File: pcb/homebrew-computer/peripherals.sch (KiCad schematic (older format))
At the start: 0 parts

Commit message: Add the memory interface logic
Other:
- note added: "This part needs to include logic for handling peripheral interrupts"
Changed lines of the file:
@@
 Comment4 ""
 $EndDescr
+Text Notes 3250 2850 0    50   Italic 0
+This part needs to include logic for handling peripheral interrupts
 $EndSCHEMATC

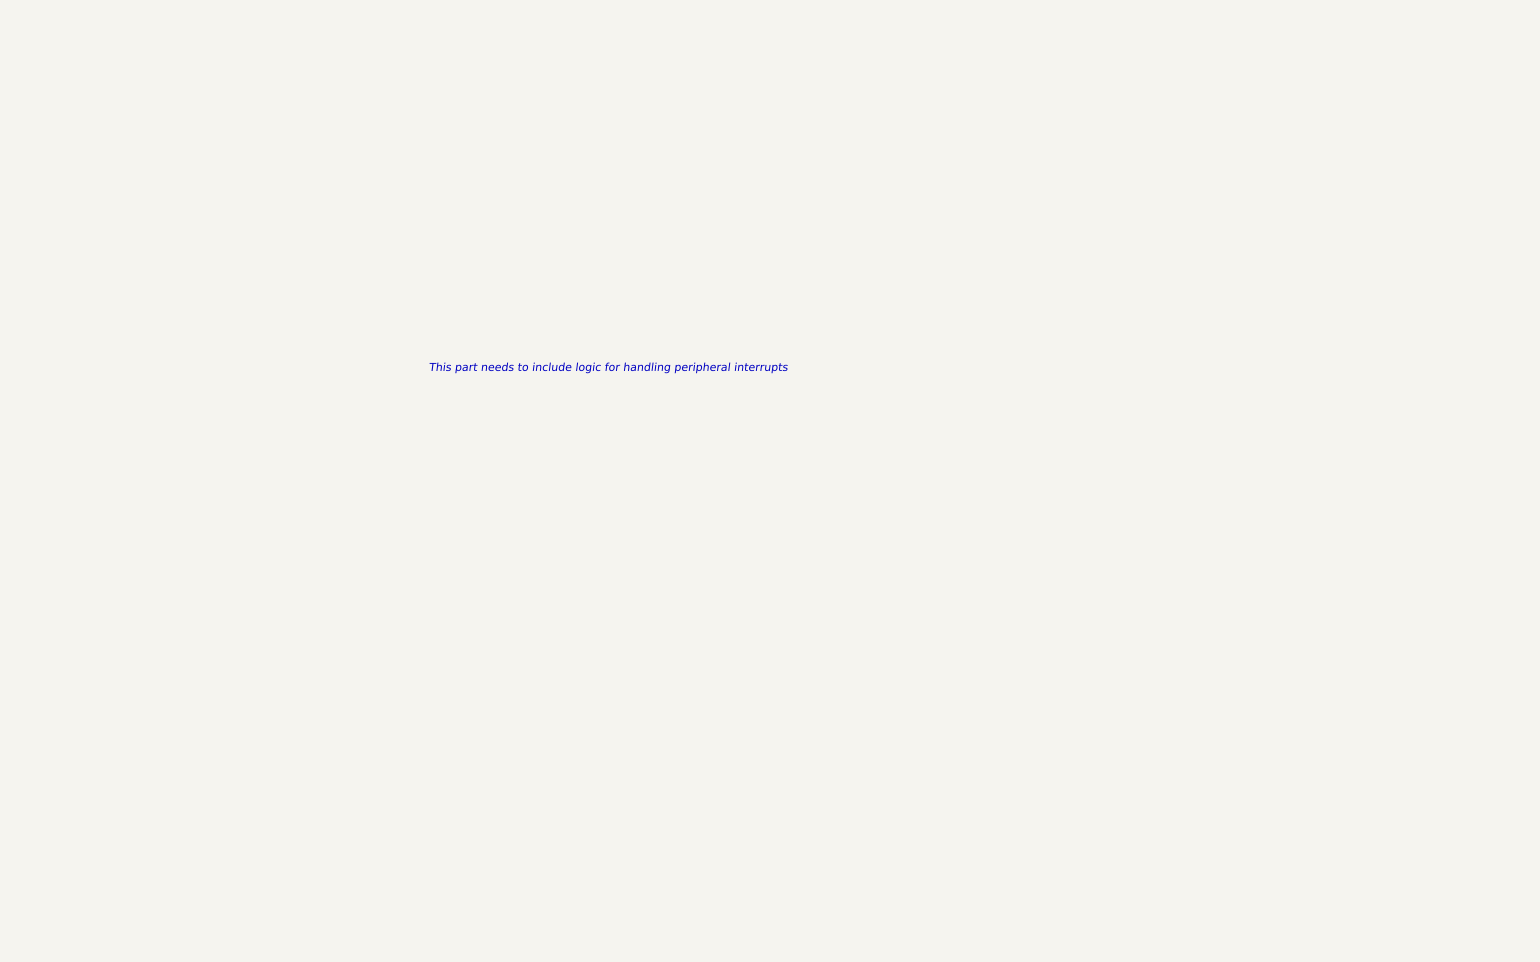
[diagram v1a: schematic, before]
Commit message: Add beginning of peripheral ios
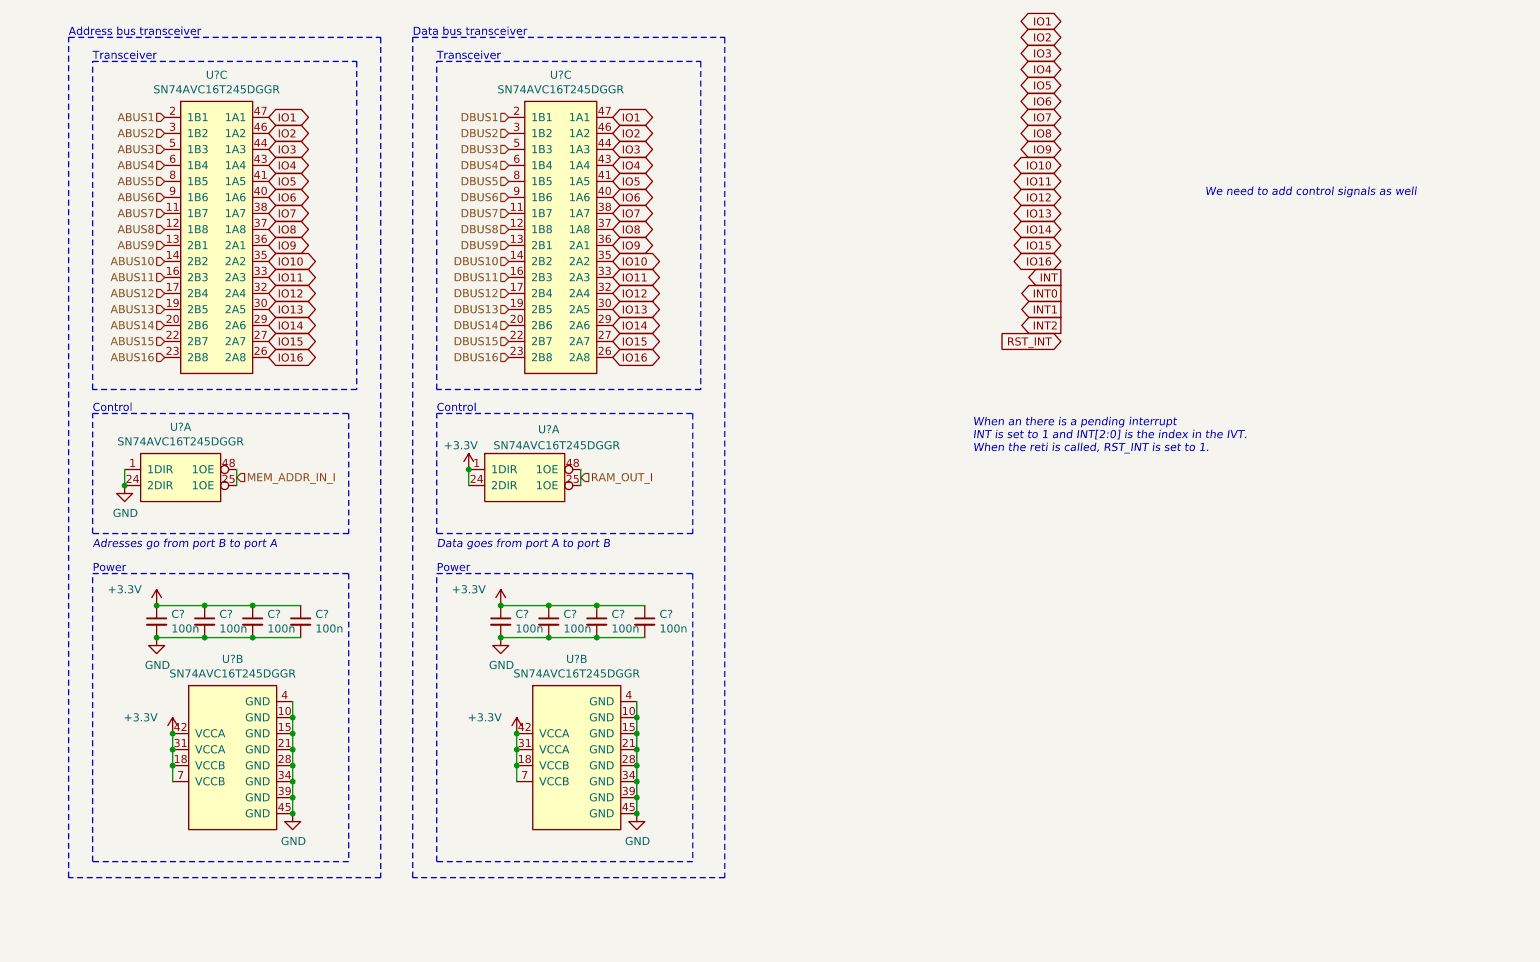
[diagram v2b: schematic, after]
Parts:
- added C? (x8): 100n, symbol Device:C_Small
- added U? (x6): SN74AVC16T245DGGR, symbol 74AVC16T245:SN74AVC16T245DGGR
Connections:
- new net +3V3: C?.1, C?.1, C?.1, C?.1, C?.1, C?.1, C?.1, C?.1, U?.1 (1DIR), U?.18 (VCCB), U?.18 (VCCB), U?.24 (2DIR), U?.31 (VCCA), U?.31 (VCCA), U?.42 (VCCA), U?.42 (VCCA), U?.7 (VCCB), U?.7 (VCCB)
- new net ABUS1: U?.2 (1B1)
- new net ABUS10: U?.14 (2B2)
- new net ABUS11: U?.16 (2B3)
- new net ABUS12: U?.17 (2B4)
- new net ABUS13: U?.19 (2B5)
- new net ABUS14: U?.20 (2B6)
- new net ABUS15: U?.22 (2B7)
- new net ABUS16: U?.23 (2B8)
- new net ABUS2: U?.3 (1B2)
- new net ABUS3: U?.5 (1B3)
- new net ABUS4: U?.6 (1B4)
- new net ABUS5: U?.8 (1B5)
- new net ABUS6: U?.9 (1B6)
- new net ABUS7: U?.11 (1B7)
- new net ABUS8: U?.12 (1B8)
- new net ABUS9: U?.13 (2B1)
- new net DBUS1: U?.2 (1B1)
- new net DBUS10: U?.14 (2B2)
- new net DBUS11: U?.16 (2B3)
- new net DBUS12: U?.17 (2B4)
- new net DBUS13: U?.19 (2B5)
- new net DBUS14: U?.20 (2B6)
- new net DBUS15: U?.22 (2B7)
- new net DBUS16: U?.23 (2B8)
- new net DBUS2: U?.3 (1B2)
- new net DBUS3: U?.5 (1B3)
- new net DBUS4: U?.6 (1B4)
- new net DBUS5: U?.8 (1B5)
- new net DBUS6: U?.9 (1B6)
- new net DBUS7: U?.11 (1B7)
- new net DBUS8: U?.12 (1B8)
- new net DBUS9: U?.13 (2B1)
- new net GND: C?.2, C?.2, C?.2, C?.2, C?.2, C?.2, C?.2, C?.2, U?.1 (1DIR), U?.10 (GND), U?.10 (GND), U?.15 (GND), U?.15 (GND), U?.21 (GND), U?.21 (GND), U?.24 (2DIR), U?.28 (GND), U?.28 (GND), U?.34 (GND), U?.34 (GND), U?.39 (GND), U?.39 (GND), U?.4 (GND), U?.4 (GND), U?.45 (GND), U?.45 (GND)
- new net IO1: U?.47 (1A1), U?.47 (1A1)
- new net IO10: U?.35 (2A2), U?.35 (2A2)
- new net IO11: U?.33 (2A3), U?.33 (2A3)
- new net IO12: U?.32 (2A4), U?.32 (2A4)
- new net IO13: U?.30 (2A5), U?.30 (2A5)
- new net IO14: U?.29 (2A6), U?.29 (2A6)
- new net IO15: U?.27 (2A7), U?.27 (2A7)
- new net IO16: U?.26 (2A8), U?.26 (2A8)
- new net IO2: U?.46 (1A2), U?.46 (1A2)
- new net IO3: U?.44 (1A3), U?.44 (1A3)
- new net IO4: U?.43 (1A4), U?.43 (1A4)
- new net IO5: U?.41 (1A5), U?.41 (1A5)
- new net IO6: U?.40 (1A6), U?.40 (1A6)
- new net IO7: U?.38 (1A7), U?.38 (1A7)
- new net IO8: U?.37 (1A8), U?.37 (1A8)
- new net IO9: U?.36 (2A1), U?.36 (2A1)
- new net MEM_ADDR_IN_I: U?.25 (1OE), U?.48 (1OE)
- new net RAM_OUT_I: U?.25 (1OE), U?.48 (1OE)
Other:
- note added: "Address bus transceiver"
- note added: "Adresses go from port B to port A"
- note added: "Control"
- note added: "Data bus transceiver"
- note added: "Data goes from port A to port B"
- note added: "Power"
- note added: "Transceiver"
- note added: "We need to add control signals as well"
- note added: "When an there is a pending interrupt\nINT is set to 1 and INT[2:0] is the index in the IVT.\nWhen the reti is called, RST_INT is set to 1."
- note removed: "This part needs to include logic for handling peripheral interrupts"

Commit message: Keep working on the peripheral interface
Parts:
- removed C? (x4): 100n, symbol Device:C_Small
- removed U? (x3): SN74AVC16T245DGGR, symbol 74AVC16T245:SN74AVC16T245DGGR
- added C? (x5): 100n, symbol Device:C_Small
- added D? (x4): D_Small, symbol Device:D_Small
- added J?: Conn_02x20_Counter_Clockwise, symbol Connector_Generic:Conn_02x20_Counter_Clockwise
- added U?: SN74AVC4T245PWR, symbol 74AVC4T245:SN74AVC4T245PWR
- added U? (x3): SN74AVC16T245DGGR, symbol 74AVC16T245:SN74AVC16T245DGGR
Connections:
- net +3V3: now also C?.1, C?.1, C?.1, C?.1, C?.1, U?.1 (1DIR), U?.1 (VCCA), U?.16 (VCCB), U?.18 (VCCB), U?.2 (1DIR), U?.24 (2DIR), U?.3 (2DIR), U?.31 (VCCA), U?.42 (VCCA), U?.7 (VCCB)
- net ABUS1: now also U?.13 (1B1)
- net ABUS2: now also U?.12 (1B2)
- net ABUS3: now also U?.11 (2B1)
- net DBUS1: now also U?.2 (1B1)
- net DBUS10: now also U?.14 (2B2)
- net DBUS11: now also U?.16 (2B3)
- net DBUS12: now also U?.17 (2B4)
- net DBUS13: now also U?.19 (2B5)
- net DBUS14: now also U?.20 (2B6)
- net DBUS15: now also U?.22 (2B7)
- net DBUS16: now also U?.23 (2B8)
- net DBUS2: now also U?.3 (1B2)
- net DBUS3: now also U?.5 (1B3)
- net DBUS4: now also U?.6 (1B4)
- net DBUS5: now also U?.8 (1B5)
- net DBUS6: now also U?.9 (1B6)
- net DBUS7: now also U?.11 (1B7)
- net DBUS8: now also U?.12 (1B8)
- net DBUS9: now also U?.13 (2B1)
- net GND: now also C?.2, C?.2, C?.2, C?.2, C?.2, J?.1 (Pin_1), J?.10 (Pin_10), J?.13 (Pin_13), J?.16 (Pin_16), J?.19 (Pin_19), J?.22 (Pin_22), J?.25 (Pin_25), J?.28 (Pin_28), J?.31 (Pin_31), J?.34 (Pin_34), J?.37 (Pin_37), J?.4 (Pin_4), J?.40 (Pin_40), J?.7 (Pin_7), U?.10 (GND), U?.15 (GND), U?.21 (GND), U?.28 (GND), U?.34 (GND), U?.39 (GND), U?.4 (GND), U?.45 (GND), U?.7 (2A2), U?.8 (GND), U?.9 (GND)
- net INT: now also J?.14 (Pin_14)
- net INT0: now also J?.15 (Pin_15), U?.4 (1A1)
- net INT1: now also J?.17 (Pin_17), U?.5 (1A2)
- net INT2: now also J?.18 (Pin_18), U?.6 (2A1)
- net IO1: now also J?.2 (Pin_2), U?.47 (1A1)
- net IO10: now also J?.30 (Pin_30), U?.35 (2A2)
- net IO11: now also J?.32 (Pin_32), U?.33 (2A3)
- net IO12: now also J?.33 (Pin_33), U?.32 (2A4)
- net IO13: now also J?.35 (Pin_35), U?.30 (2A5)
- net IO14: now also J?.36 (Pin_36), U?.29 (2A6)
- net IO15: now also J?.38 (Pin_38), U?.27 (2A7)
- net IO16: now also J?.39 (Pin_39), U?.26 (2A8)
- net IO2: now also J?.3 (Pin_3), U?.46 (1A2)
- net IO3: now also J?.5 (Pin_5), U?.44 (1A3)
- net IO4: now also J?.6 (Pin_6), U?.43 (1A4)
- net IO5: now also J?.8 (Pin_8), U?.41 (1A5)
- net IO6: now also J?.9 (Pin_9), U?.40 (1A6)
- net IO7: now also J?.11 (Pin_11), U?.38 (1A7)
- net IO8: now also J?.12 (Pin_12), U?.37 (1A8)
- net IO9: now also J?.29 (Pin_29), U?.36 (2A1)
- net RST_INT: now also J?.20 (Pin_20)
- net MEM_ADDR_IN_I renamed IO_ADDR_IN_I
- net IO_ADDR_IN_I: now also J?.27 (Pin_27)
- new net: D?.1 (K), D?.1 (K), D?.1 (K), D?.1 (K), U?.25 (1OE), U?.48 (1OE)
- new net INT_OUT_I: U?.14 (2OE), U?.15 (1OE)
- new net IO_INB_I: D?.2 (A), J?.21 (Pin_21)
- new net IO_IN_I: D?.2 (A), J?.24 (Pin_24)
- new net IO_OUTB_I: D?.2 (A), J?.23 (Pin_23)
- new net IO_OUT_I: D?.2 (A), J?.26 (Pin_26)
- no-connect marks 0 -> 1
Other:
- note added: "Data goes from port A to port B\nWe use diodes to implement the OR\nfunction as there will only be one \nactive at the same time"
- note added: "Information goes from A to B,\nso DIR is tied to 3.3v"
- note added: "Interrupt bus transceiver"
- note added: "Peripheral connector"
- note added: "The clock is not sent through this connector.\nIt is passed by another connector to the clock module,\nin the external clock configuration"
- note added: "These connections can change\nto make routing easier"
- note added: "We need to care about ground return path.\nIt doesn’t have to be perfect, but we should\ninclude at least a few ground connections"
- note removed: "Data goes from port A to port B"
- note removed: "We need to add control signals as well"
- moved on the sheet: C?, U?A, U?B, U?C

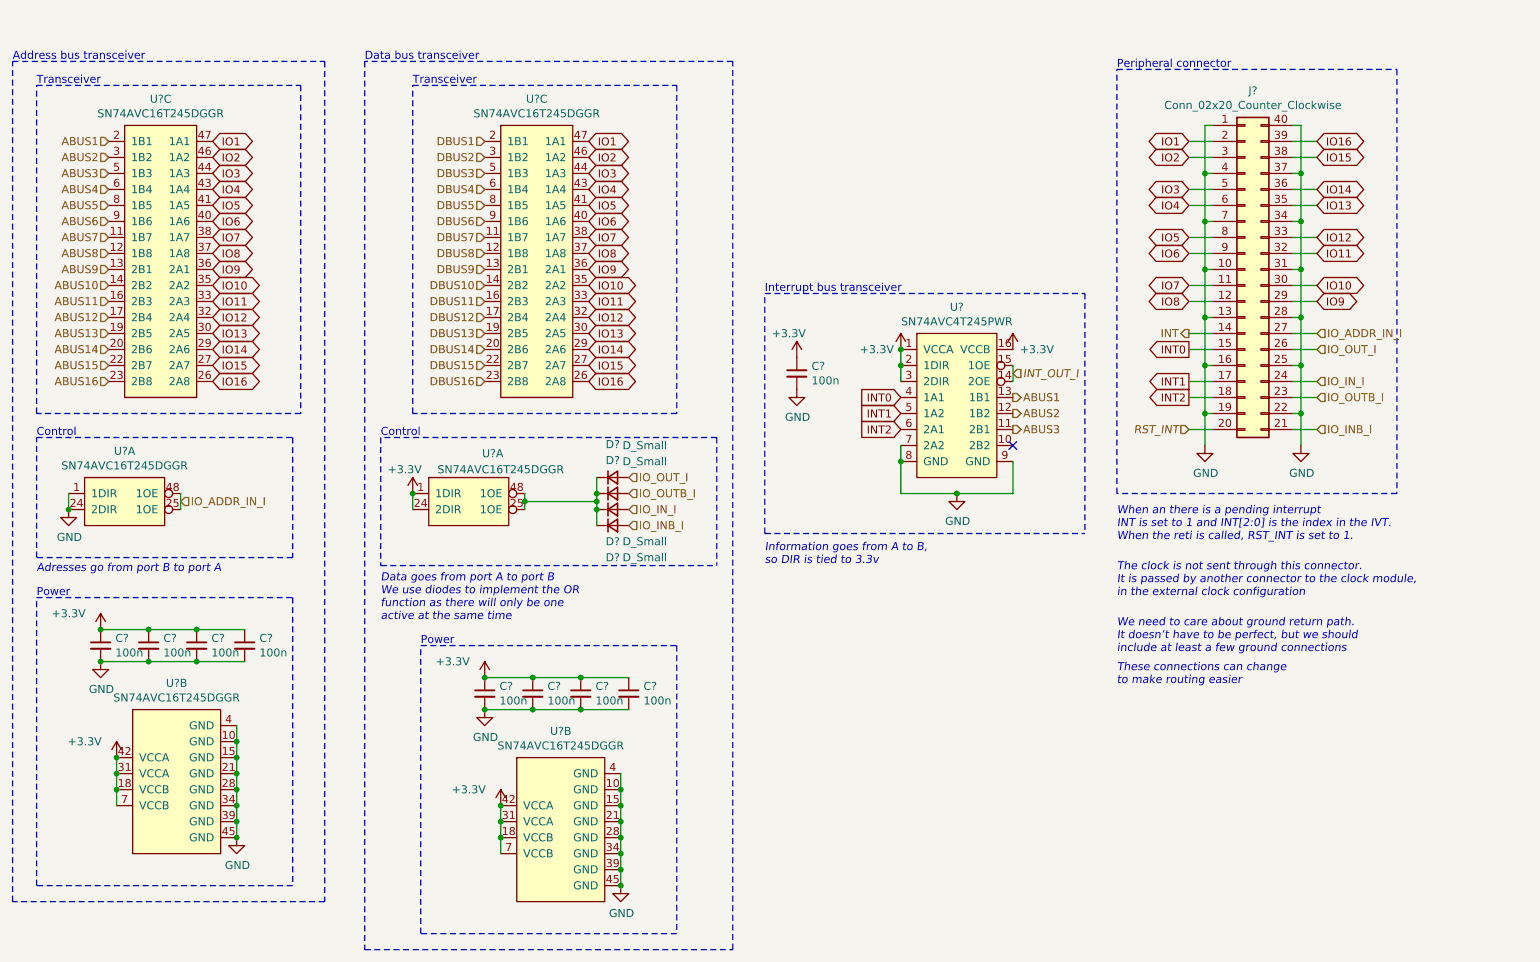
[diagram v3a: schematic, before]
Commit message: Remove the address bus as it would require too big of a connector
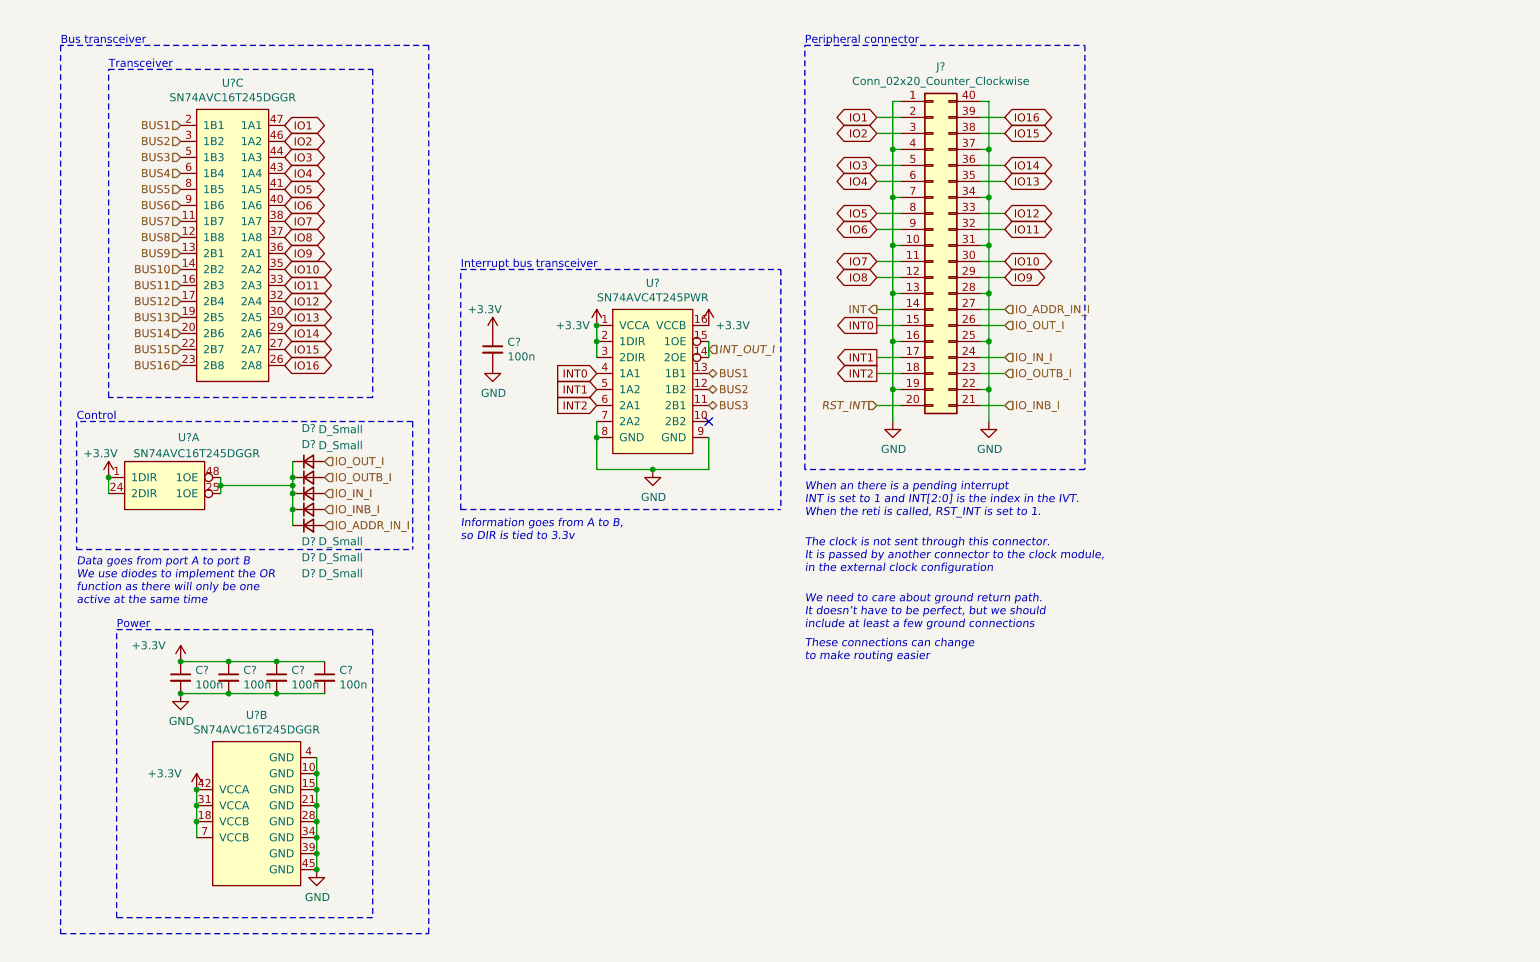
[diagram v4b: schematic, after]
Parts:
- removed C? (x8): 100n, symbol Device:C_Small
- removed D? (x4): D_Small, symbol Device:D_Small
- removed U? (x6): SN74AVC16T245DGGR, symbol 74AVC16T245:SN74AVC16T245DGGR
- added C? (x4): 100n, symbol Device:C_Small
- added D? (x5): D_Small, symbol Device:D_Small
- added U? (x3): SN74AVC16T245DGGR, symbol 74AVC16T245:SN74AVC16T245DGGR
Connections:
- net +3V3: now also C?.1, C?.1, C?.1, C?.1, U?.1 (1DIR), U?.18 (VCCB), U?.24 (2DIR), U?.31 (VCCA), U?.42 (VCCA), U?.7 (VCCB)
- net GND: now also C?.2, C?.2, C?.2, C?.2, U?.10 (GND), U?.15 (GND), U?.21 (GND), U?.28 (GND), U?.34 (GND), U?.39 (GND), U?.4 (GND), U?.45 (GND)
- net IO1: now also U?.47 (1A1)
- net IO10: now also U?.35 (2A2)
- net IO11: now also U?.33 (2A3)
- net IO12: now also U?.32 (2A4)
- net IO13: now also U?.30 (2A5)
- net IO14: now also U?.29 (2A6)
- net IO15: now also U?.27 (2A7)
- net IO16: now also U?.26 (2A8)
- net IO2: now also U?.46 (1A2)
- net IO3: now also U?.44 (1A3)
- net IO4: now also U?.43 (1A4)
- net IO5: now also U?.41 (1A5)
- net IO6: now also U?.40 (1A6)
- net IO7: now also U?.38 (1A7)
- net IO8: now also U?.37 (1A8)
- net IO9: now also U?.36 (2A1)
- net IO_ADDR_IN_I: now also D?.2 (A)
- net IO_INB_I: now also D?.2 (A)
- net IO_IN_I: now also D?.2 (A)
- net IO_OUTB_I: now also D?.2 (A)
- net IO_OUT_I: now also D?.2 (A)
- net ABUS1 renamed BUS1
- net BUS1: now also U?.2 (1B1)
- net ABUS2 renamed BUS2
- net BUS2: now also U?.3 (1B2)
- net ABUS3 renamed BUS3
- net BUS3: now also U?.5 (1B3)
- new net: D?.1 (K), D?.1 (K), D?.1 (K), D?.1 (K), D?.1 (K), U?.25 (1OE), U?.48 (1OE)
- new net BUS10: U?.14 (2B2)
- new net BUS11: U?.16 (2B3)
- new net BUS12: U?.17 (2B4)
- new net BUS13: U?.19 (2B5)
- new net BUS14: U?.20 (2B6)
- new net BUS15: U?.22 (2B7)
- new net BUS16: U?.23 (2B8)
- new net BUS4: U?.6 (1B4)
- new net BUS5: U?.8 (1B5)
- new net BUS6: U?.9 (1B6)
- new net BUS7: U?.11 (1B7)
- new net BUS8: U?.12 (1B8)
- new net BUS9: U?.13 (2B1)
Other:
- note added: "Bus transceiver"
- note removed: "Address bus transceiver"
- note removed: "Adresses go from port B to port A"
- note removed: "Data bus transceiver"
- moved on the sheet: C?, J?, U?
